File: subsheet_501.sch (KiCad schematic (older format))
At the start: 11 parts, among them P500 4K7 ×8, P501 4K7 ×8, P502 4K7 ×8, U509 74LS244_PHY, U510 74LS244_PHY, U511 74LS373_PHY, U512 74LS244_PHY

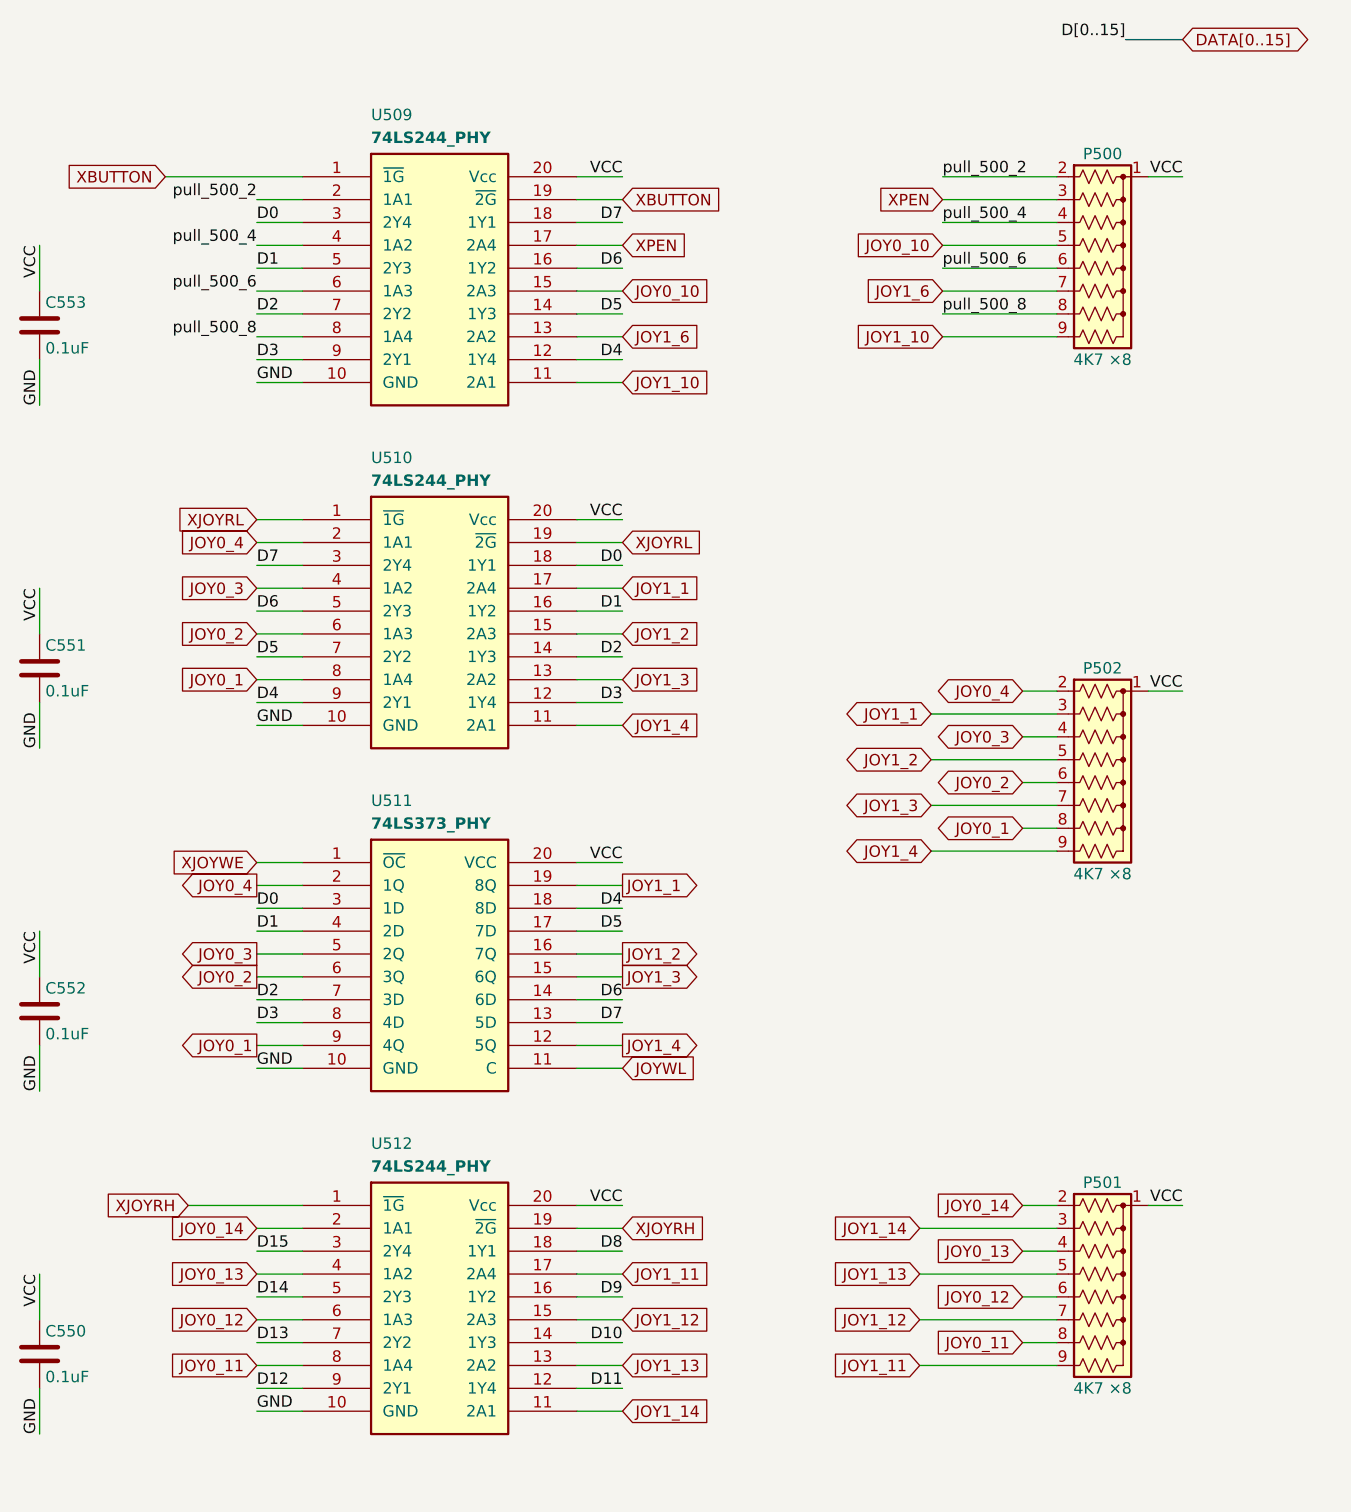
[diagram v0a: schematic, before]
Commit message: [Schematic] Fixed again resistors connected to L500 and L501
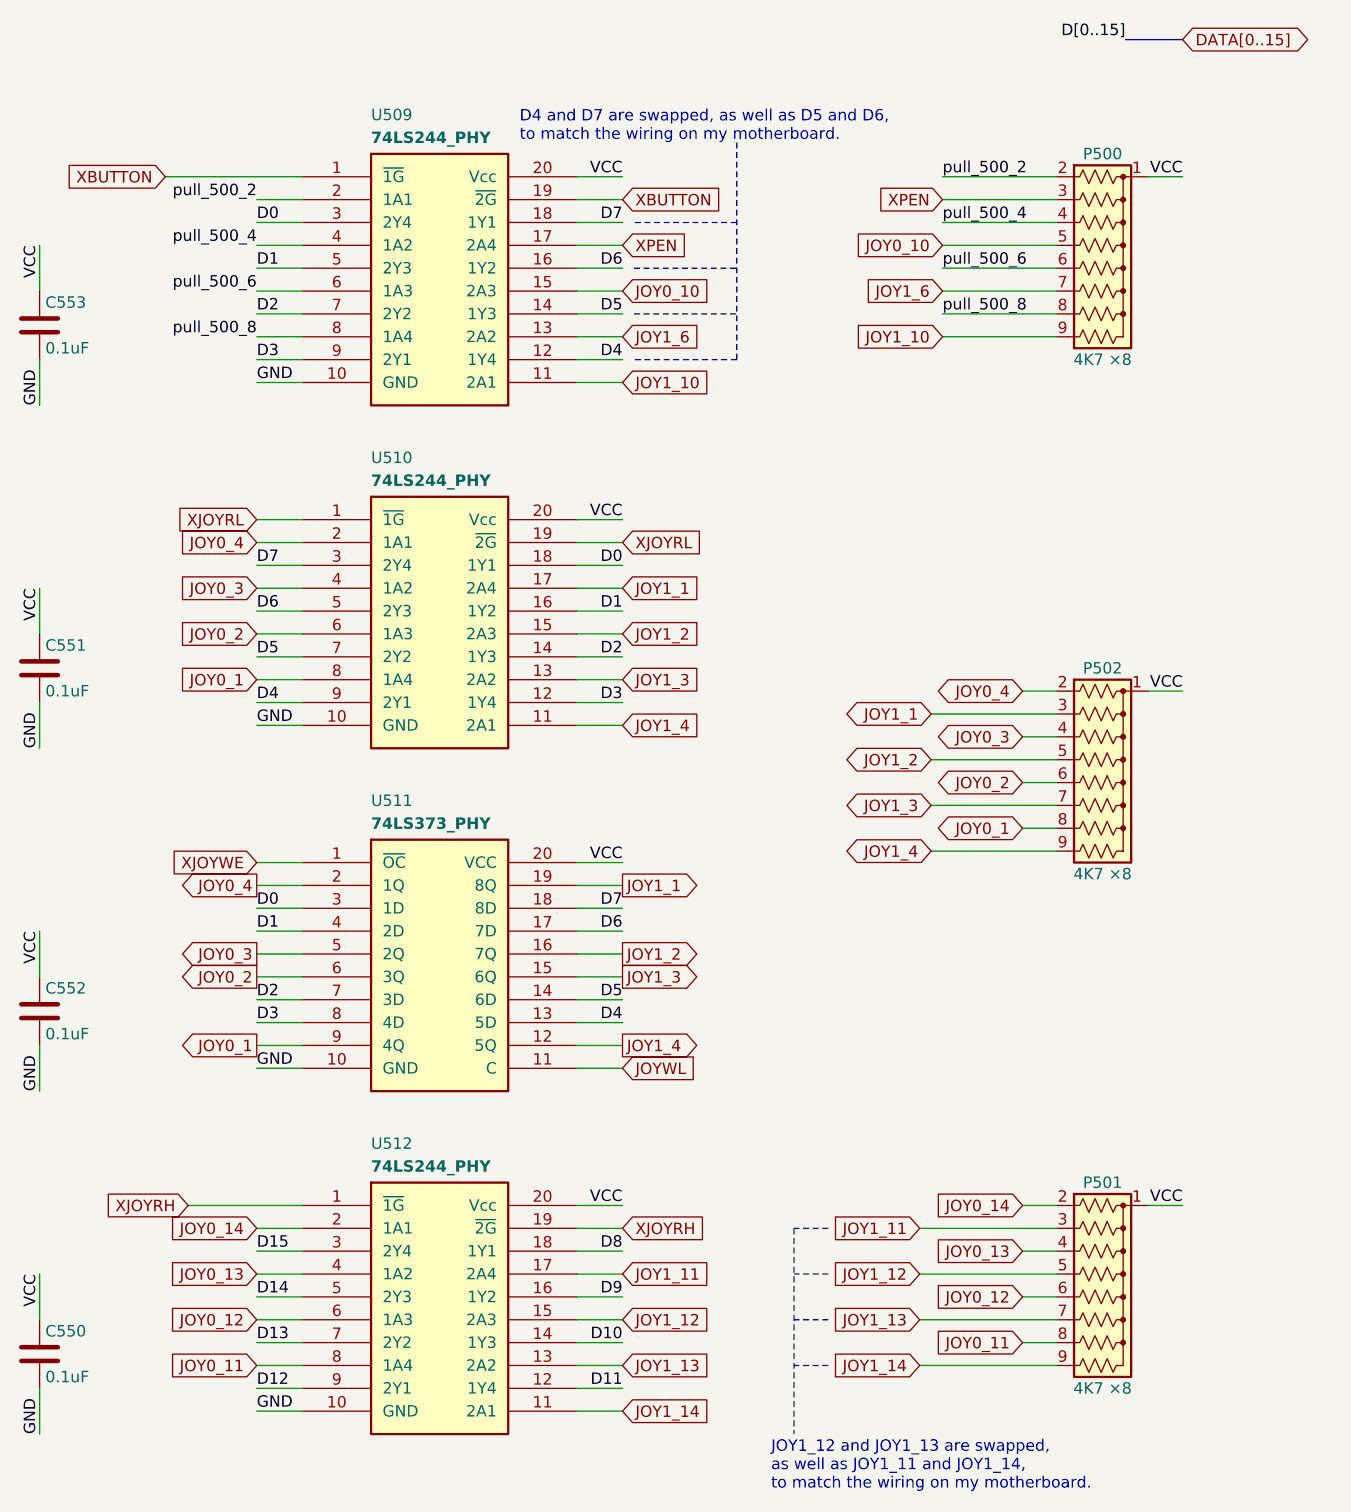
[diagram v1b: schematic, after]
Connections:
- net D4: now also U511.13 (5D); no longer U511.18 (8D)
- net D5: now also U511.14 (6D); no longer U511.17 (7D)
- net D6: now also U511.17 (7D); no longer U511.14 (6D)
- net D7: now also U511.18 (8D); no longer U511.13 (5D)
- net JOY1_11: now also P501.3 (R2); no longer P501.9 (R8)
- net JOY1_12: now also P501.5 (R4); no longer P501.7 (R6)
- net JOY1_13: now also P501.7 (R6); no longer P501.5 (R4)
- net JOY1_14: now also P501.9 (R8); no longer P501.3 (R2)
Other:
- note added: "D4 and D7 are swapped, as well as D5 and D6,\nto match the wiring on my motherboard.\n"
- note added: "JOY1_12 and JOY1_13 are swapped,\nas well as JOY1_11 and JOY1_14,\nto match the wiring on my motherboard.\n"
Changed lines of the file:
@@
 Text Label 2700 5300 0    50   ~ 0
 D3
-Text Label 4300 4800 2    50   ~ 0
-D4
-Text Label 4300 4900 2    50   ~ 0
-D5
-Text Label 4300 5200 2    50   ~ 0
-D6
-Text Label 4300 5300 2    50   ~ 0
-D7
 Wire Wire Line
 	2700 5500 2900 5500
@@
 Text GLabel 6050 6700 0    50   Input ~ 0
 JOY0_11
+Text GLabel 5600 6800 0    50   Input ~ 0
+JOY1_14
+Text GLabel 5600 6600 0    50   Input ~ 0
+JOY1_13
+Text GLabel 5600 6400 0    50   Input ~ 0
+JOY1_12
 Text GLabel 5600 6200 0    50   Input ~ 0
-JOY1_14
-Text GLabel 5600 6400 0    50   Input ~ 0
-JOY1_13
-Text GLabel 5600 6600 0    50   Input ~ 0
-JOY1_12
-Text GLabel 5600 6800 0    50   Input ~ 0
 JOY1_11
 Wire Wire Line
@@
 Wire Wire Line
 	1750 6900 1750 7100
+Text Notes 4950 7350 0    50   ~ 0
+JOY1_12 and JOY1_13 are swapped,\nas well as JOY1_11 and JOY1_14,\nto match the wiring on my motherboard.\n
+Text Notes 3850 1450 0    50   ~ 0
+D4 and D7 are swapped, as well as D5 and D6,\nto match the wiring on my motherboard.\n
+Wire Notes Line
+	4800 2400 4350 2400
+Wire Notes Line
+	4800 1450 4800 2400
+Wire Notes Line
+	4800 1800 4350 1800
+Wire Notes Line
+	4350 2000 4800 2000
+Wire Notes Line
+	4350 2200 4800 2200
+Wire Notes Line
+	5200 6200 5050 6200
+Wire Notes Line
+	5200 6400 5050 6400
+Wire Notes Line
+	5200 6600 5050 6600
+Wire Notes Line
+	5200 6800 5050 6800
+Wire Notes Line
+	5050 6200 5050 7100
+Text Label 4300 4800 2    50   ~ 0
+D7
+Text Label 4300 4900 2    50   ~ 0
+D6
+Text Label 4300 5200 2    50   ~ 0
+D5
+Text Label 4300 5300 2    50   ~ 0
+D4
 $EndSCHEMATC

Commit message: [Schematics] add comments to match wiring changes in extended game ports controllers
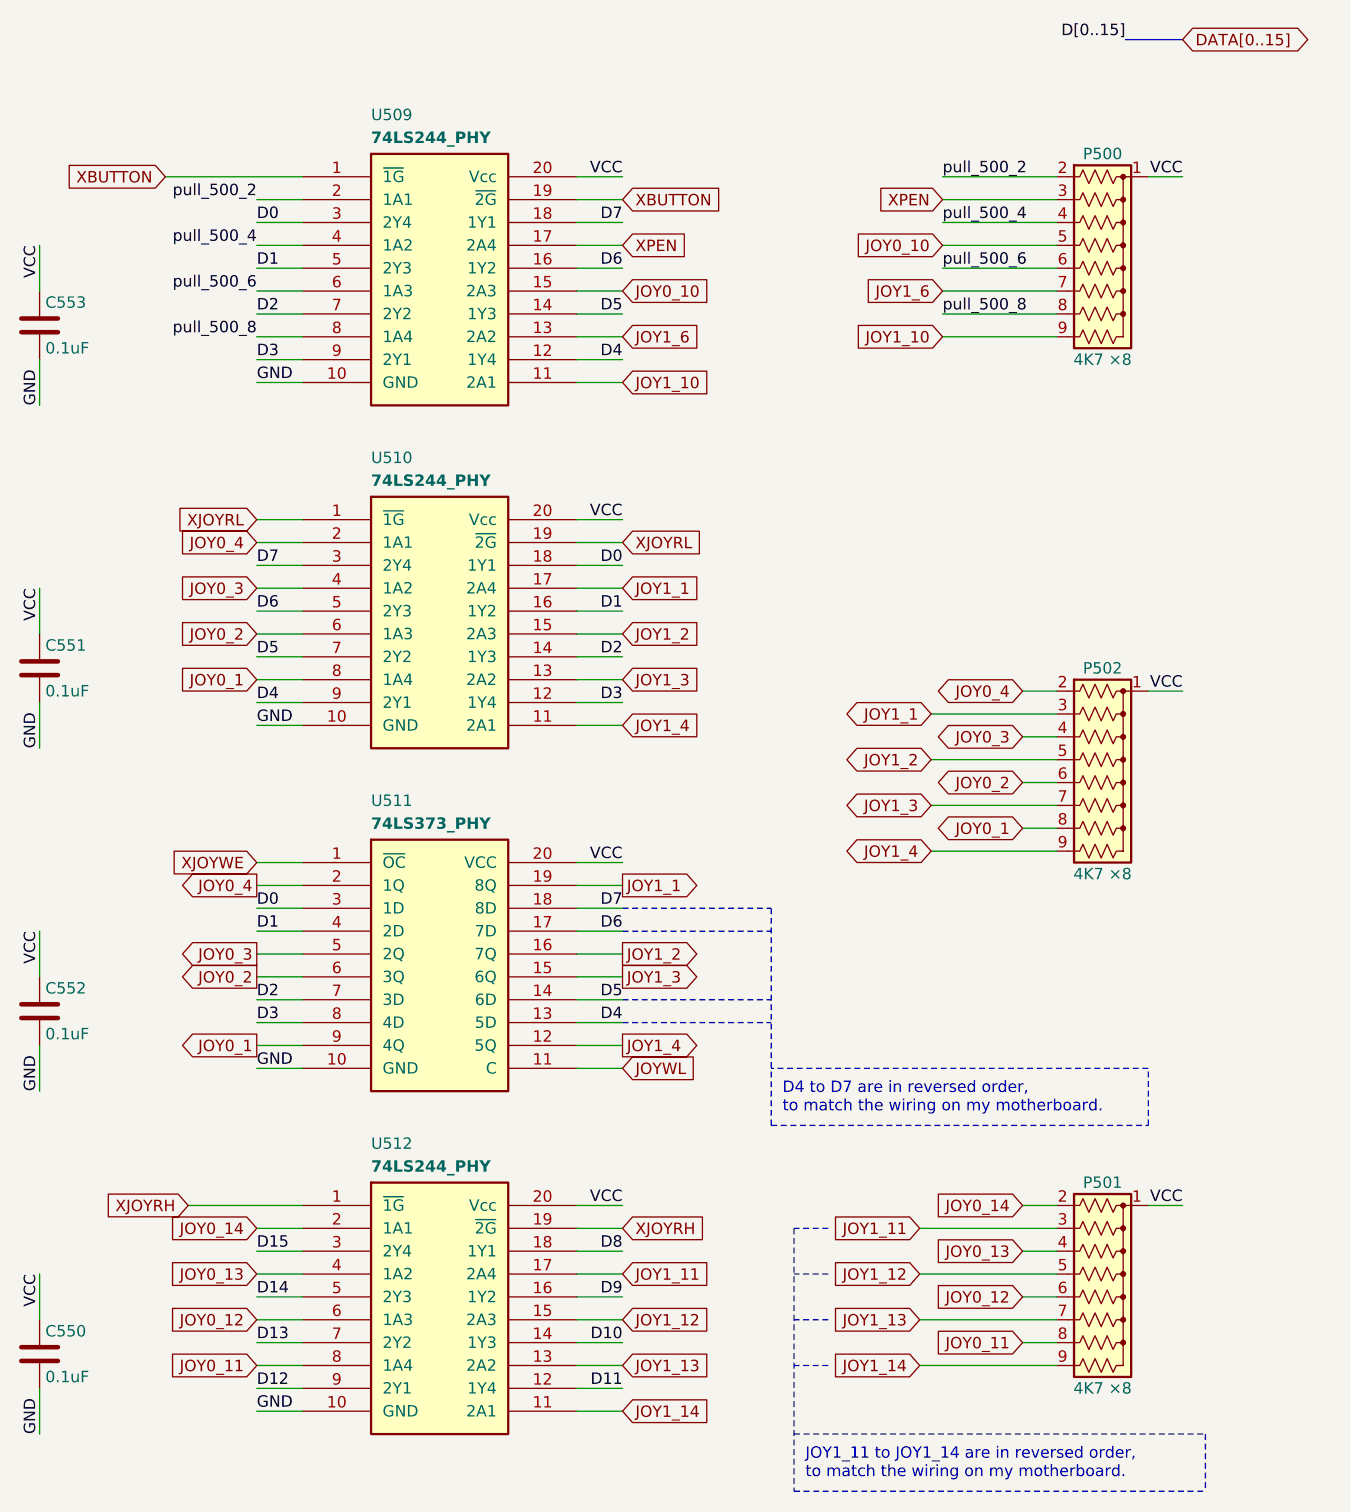
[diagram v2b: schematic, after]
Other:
- note added: "D4 to D7 are in reversed order,\nto match the wiring on my motherboard.\n"
- note added: "JOY1_11 to JOY1_14 are in reversed order,\nto match the wiring on my motherboard.\n"
- note removed: "D4 and D7 are swapped, as well as D5 and D6,\nto match the wiring on my motherboard.\n"
- note removed: "JOY1_12 and JOY1_13 are swapped,\nas well as JOY1_11 and JOY1_14,\nto match the wiring on my motherboard.\n"
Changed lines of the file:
@@
 Wire Wire Line
 	1750 6900 1750 7100
-Text Notes 4950 7350 0    50   ~ 0
-JOY1_12 and JOY1_13 are swapped,\nas well as JOY1_11 and JOY1_14,\nto match the wiring on my motherboard.\n
-Text Notes 3850 1450 0    50   ~ 0
-D4 and D7 are swapped, as well as D5 and D6,\nto match the wiring on my motherboard.\n
-Wire Notes Line
-	4800 2400 4350 2400
-Wire Notes Line
-	4800 1450 4800 2400
-Wire Notes Line
-	4800 1800 4350 1800
-Wire Notes Line
-	4350 2000 4800 2000
-Wire Notes Line
-	4350 2200 4800 2200
+Text Notes 5100 7300 0    50   ~ 0
+JOY1_11 to JOY1_14 are in reversed order,\nto match the wiring on my motherboard.\n
 Wire Notes Line
 	5200 6200 5050 6200
@@
 Wire Notes Line
 	5200 6800 5050 6800
-Wire Notes Line
-	5050 6200 5050 7100
 Text Label 4300 4800 2    50   ~ 0
 D7
@@
 Text Label 4300 5300 2    50   ~ 0
 D4
+Text Notes 5000 5700 0    50   ~ 0
+D4 to D7 are in reversed order,\nto match the wiring on my motherboard.\n
+Wire Notes Line
+	5050 7350 6850 7350
+Wire Notes Line
+	5050 6200 5050 7350
+Wire Notes Line
+	6850 7100 6850 7350
+Wire Notes Line
+	5050 7100 6850 7100
+Wire Notes Line
+	6600 5750 6600 5500
+Wire Notes Line
+	6600 5500 4950 5500
+Wire Notes Line
+	4950 5750 6600 5750
+Wire Notes Line
+	4300 4800 4950 4800
+Wire Notes Line
+	4300 4900 4950 4900
+Wire Notes Line
+	4300 5200 4950 5200
+Wire Notes Line
+	4300 5300 4950 5300
+Wire Notes Line
+	4950 4800 4950 5750
 $EndSCHEMATC
